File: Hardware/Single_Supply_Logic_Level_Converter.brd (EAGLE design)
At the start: 27.9 x 29.2 mm, 81 parts, among them U1 TXB0104, U2 TPS61200, U3 ADJ

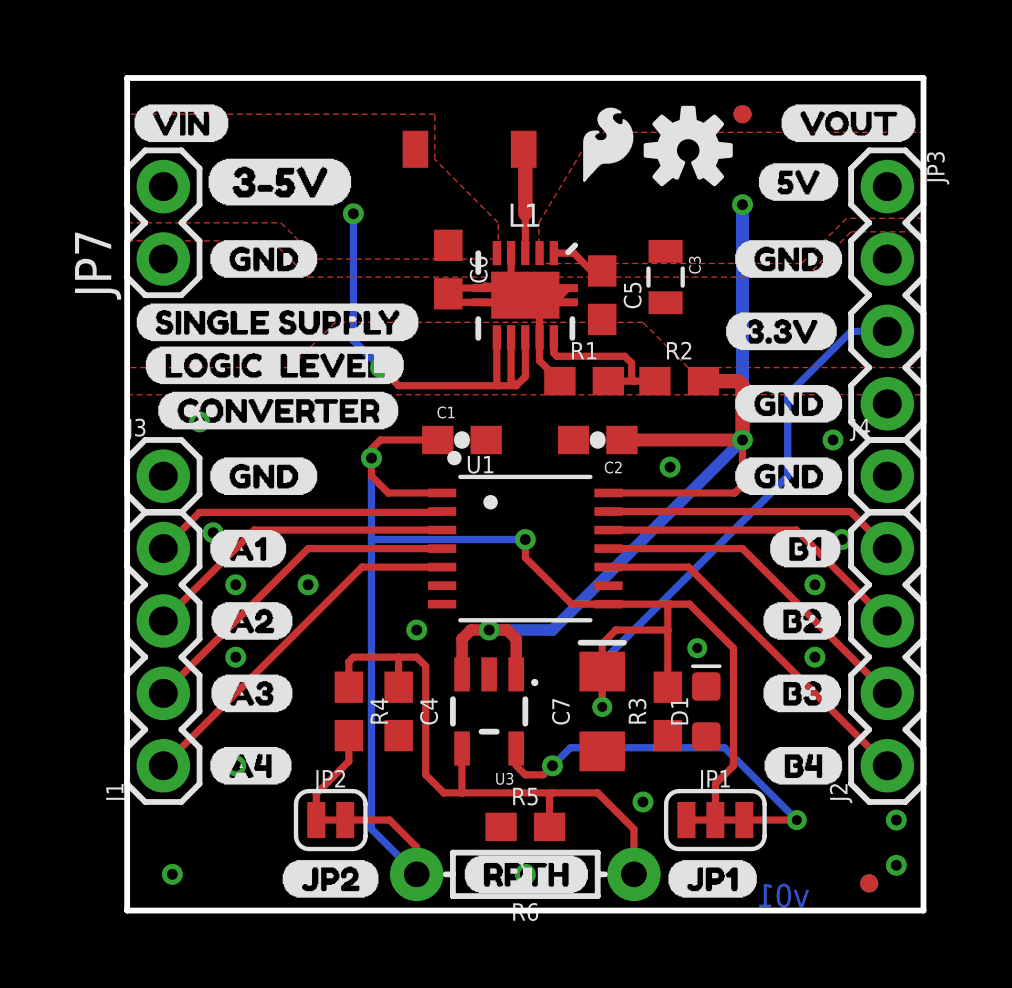
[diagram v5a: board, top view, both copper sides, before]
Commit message: Added text for warnings and jumper settings
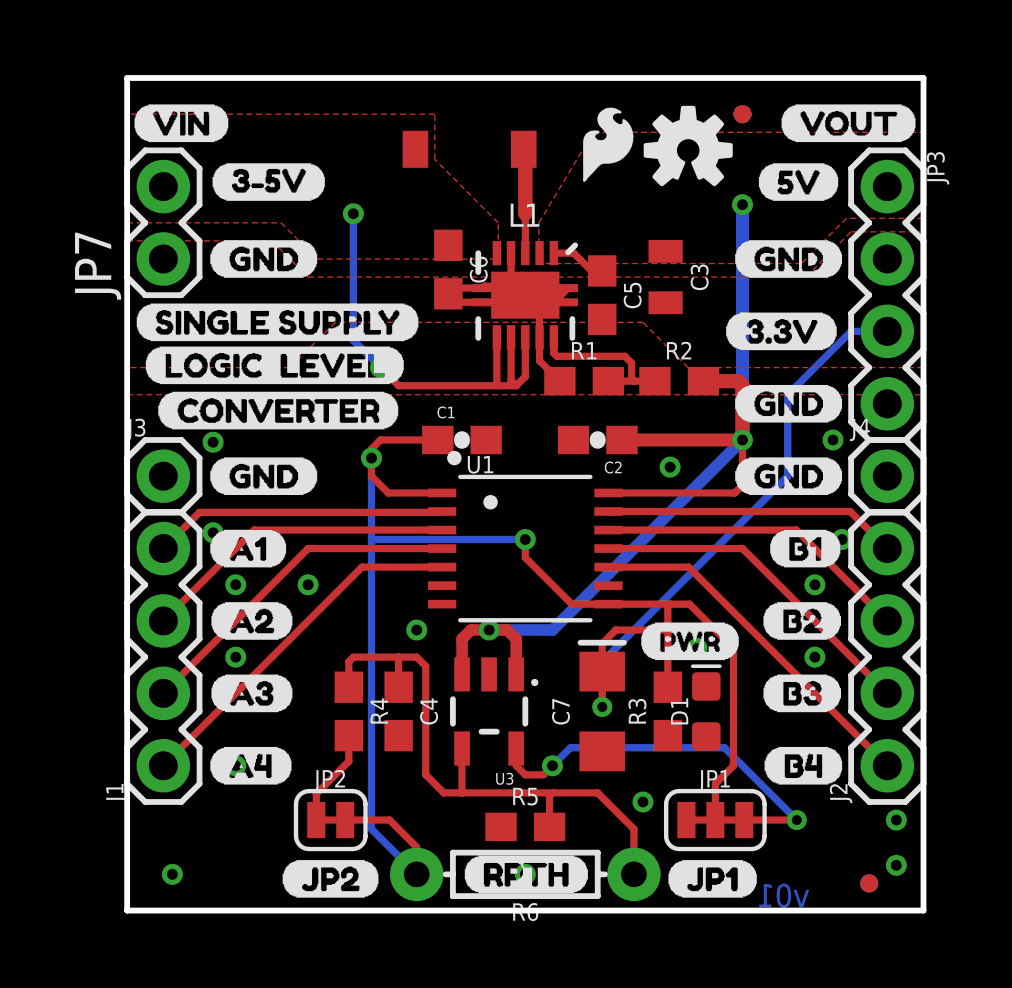
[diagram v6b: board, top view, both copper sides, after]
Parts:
- C3: device CH_passive:0805 -> SparkFun-Capacitors:0805
- U$25: device voltageIn:3#5V0 -> buzzard_labels (22):3#5V1
- U$29: device voltageIn:3#5V0 -> buzzard_labels (24):PWR0
- moved U$29 19.0 mm to (17.9, 9.45), flipped to the top
- moved U$25 0.16 mm to (2.94, 25.6)
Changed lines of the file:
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@@
 </autorouter>
 <elements>
-<element name="U1" library="SparkFun-IC-Comms" library_urn="urn:adsk.eagle:library:521" package="TSSOP14" package3d_urn="urn:adsk.eagle:package:38732/1" value="TXB0104" x="13.97" y="12.7" rot="R270">
-<attribute name="PROD_ID" value="NA-XXXXX" x="1.27" y="-5.08" size="1.778" layer="27" rot="R270" display="off"/>
+<element name="U1" library="SparkFun-IC-Comms" package="TSSOP14" value="TXB0104" x="13.97" y="12.7" rot="R270">
+<attribute name="PROD_ID" value="IC-13929" x="1.27" y="-5.08" size="1.778" layer="27" rot="R270" display="off"/>
 <attribute name="VALUE" value="TXB0104" x="13.97" y="12.7" size="1.778" layer="27" rot="R270" display="off"/>
 </element>
@@
 <attribute name="PROD_ID" value="CAP-00810" x="-2.54" y="40.64" size="1.778" layer="27" rot="R180" display="off"/>
 </element>
-<element name="C3" library="CH_passive" package="0805" value="22uF" x="18.89125" y="22.225" rot="R270"/>
+<element name="C3" library="SparkFun-Capacitors" package="0805" value="22uF" x="18.89125" y="22.225" rot="R270">
+<attribute name="PROD_ID" value="CAP-08402" x="18.89125" y="22.225" size="1.778" layer="27" rot="R270" display="off"/>
+<attribute name="VALUE" value="22uF" x="18.89125" y="22.225" size="1.778" layer="27" rot="R270" display="off"/>
+</element>
 <element name="U2" library="SparkFun-IC-Power" package="QFN-10_PAD" value="TPS61200" x="13.97" y="21.59" rot="R180">
 <attribute name="PROD_ID" value="IC-10035" x="13.97" y="21.59" size="1.778" layer="27" rot="R180" display="off"/>
 </element>
 <element name="C5" library="SparkFun-Capacitors" package="0603" value="0.1uF" x="16.66875" y="21.59" rot="R270">
-<attribute name="PROD_ID" value="CAP-08604" x="16.66875" y="21.59" size="1.778" layer="27" rot="R270" display="off"/>
+<attribute name="PROD_ID" value="CAP-00810" x="16.66875" y="21.59" size="1.778" layer="27" rot="R270" display="off"/>
 <attribute name="VALUE" value="0.1uF" x="16.66875" y="21.59" size="1.778" layer="27" rot="R270" display="off"/>
 </element>
@@
 </element>
 <element name="R4" library="SparkFun-Resistors" package="0603" value="13k" x="7.77875" y="6.985" rot="R270">
-<attribute name="PROD_ID" value="RES-09571" x="7.77875" y="6.985" size="1.778" layer="27" rot="R270" display="off"/>
+<attribute name="PROD_ID" value="RES-14017" x="7.77875" y="6.985" size="1.778" layer="27" rot="R270" display="off"/>
 </element>
 <element name="R5" library="SparkFun-Resistors" package="0603" value="22k" x="13.97" y="2.936875">
@@
 <element name="U$52" library="Single_Supply_Logic_Level_Converter_Lables" package="VOUT2" value="" x="27.78125" y="27.6225" rot="MR0"/>
 <element name="U$53" library="Single_Supply_Logic_Level_Converter_Lables" package="SINGLE_SUPPLY17" value="" x="18.335625" y="18.0975" rot="MR0"/>
-<element name="U$25" library="voltageIn" package="3#5V0" value="" x="2.778125" y="25.55875"/>
-<element name="U$29" library="voltageIn" package="3#5V0" value="" x="7.9375" y="25.55875" rot="MR0"/>
+<element name="U$25" library="buzzard_labels (22)" package="3#5V1" value="" x="2.936875" y="25.55875"/>
+<element name="U$29" library="buzzard_labels (24)" package="PWR0" value="" x="17.93875" y="9.445625"/>
 </elements>
 <signals>
@@
 <wire x1="15.47" y1="21.34" x2="14.5375" y2="21.34" width="0.254" layer="1"/>
 <wire x1="14.5375" y1="21.34" x2="14.2875" y2="21.59" width="0.254" layer="1"/>
-<via x="2.54" y="17.145" extent="1-16" drill="0.381"/>
+<via x="3.01625" y="16.430625" extent="1-16" drill="0.381"/>
 <via x="19.05" y="15.5575" extent="1-16" drill="0.381"/>
 <via x="24.765" y="16.51" extent="1-16" drill="0.381"/>

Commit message: adding buzzard labels
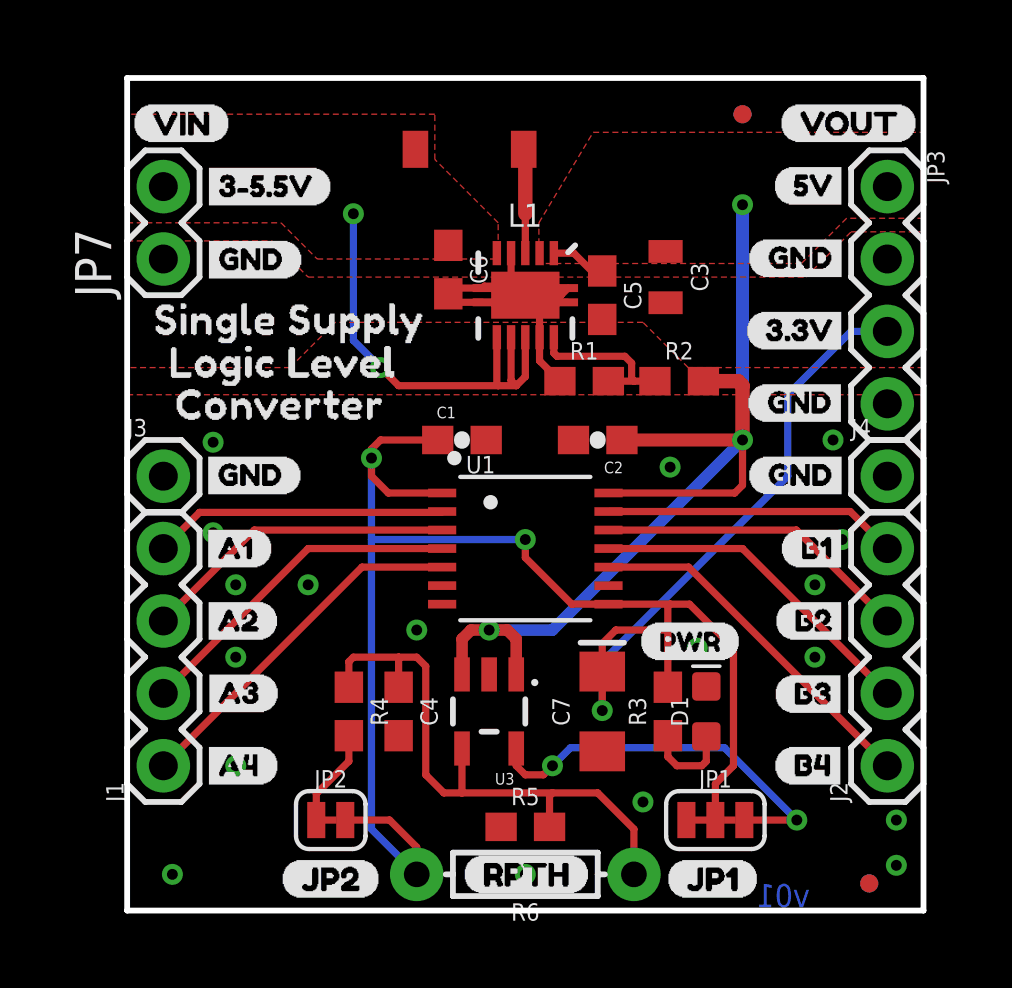
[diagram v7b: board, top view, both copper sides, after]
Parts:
- removed LOGO3: SFE_LOGO_FLAME.1_INCH, SparkFun-Aesthetics:SFE_LOGO_FLAME_.1
- removed LOGO4: OSHW-LOGOS, SparkFun-Aesthetics:OSHW-LOGO-S
- removed U$47, U$48, U$50: (no value), Single_Supply_Logic_Level_Converter_Lables:GND0
- removed U$49: (no value), Single_Supply_Logic_Level_Converter_Lables:3#3V20
- removed U$51: (no value), Single_Supply_Logic_Level_Converter_Lables:5V3
- removed U$53: (no value), Single_Supply_Logic_Level_Converter_Lables:SINGLE_SUPPLY17
- added U$34: (no value), buzzard_labels (49):A10
- added U$54: (no value), buzzard_labels (38):B19
- added U$55: (no value), buzzard_labels (38):B210
- added U$56: (no value), buzzard_labels (38):B311
- added U$57: (no value), buzzard_labels (38):B412
- added U$59: (no value), buzzard_labels (43):B13
- added U$61: (no value), buzzard_labels (43):B34
- U$10: device Single_Supply_Logic_Level_Converter_Lables:A16 -> buzzard_labels (42):CONVERTER0
- U$11: device Single_Supply_Logic_Level_Converter_Lables:A27 -> buzzard_labels (42):LOGIC_LEVEL2
- U$12: device Single_Supply_Logic_Level_Converter_Lables:A38 -> buzzard_labels (42):SINGLE_SUPPLY1
- U$13: device Single_Supply_Logic_Level_Converter_Lables:A49 -> buzzard_labels (38):GND3
- U$14: device Single_Supply_Logic_Level_Converter_Lables:B110 -> buzzard_labels (38):GND0
- U$15: device Single_Supply_Logic_Level_Converter_Lables:B211 -> buzzard_labels (38):GND3
- U$16: device Single_Supply_Logic_Level_Converter_Lables:B312 -> buzzard_labels (43):3#3V2
- U$17: device Single_Supply_Logic_Level_Converter_Lables:B413 -> buzzard_labels (43):3#5#5V6
- U$18: device Single_Supply_Logic_Level_Converter_Lables:CONVERTER19 -> buzzard_labels (38):3#3V4
- U$19: device Single_Supply_Logic_Level_Converter_Lables:GND0 -> buzzard_labels (38):5V2
- U$22: device Single_Supply_Logic_Level_Converter_Lables:LOGIC__LEVEL18 -> buzzard_labels (38):GND0
- U$24: device Single_Supply_Logic_Level_Converter_Lables:SINGLE_SUPPLY17 -> buzzard_labels (38):GND3
- U$25: device buzzard_labels (22):3#5V1 -> buzzard_labels (38):GND3
- U$26: device Single_Supply_Logic_Level_Converter_Lables:GND0 -> buzzard_labels (38):A15
- U$30: device Single_Supply_Logic_Level_Converter_Lables:GND0 -> buzzard_labels (38):A26
- U$31: device Single_Supply_Logic_Level_Converter_Lables:GND0 -> buzzard_labels (38):A37
- U$32: device Single_Supply_Logic_Level_Converter_Lables:GND0 -> buzzard_labels (38):A48
- U$33: device Single_Supply_Logic_Level_Converter_Lables:GND0 -> buzzard_labels (43):5V10
- U$35: device Single_Supply_Logic_Level_Converter_Lables:LOGIC__LEVEL18 -> buzzard_labels (49):A21
- U$36: device Single_Supply_Logic_Level_Converter_Lables:CONVERTER19 -> buzzard_labels (46):B43
- U$37: device Single_Supply_Logic_Level_Converter_Lables:GND0 -> buzzard_labels (46):B21
- U$38: device Single_Supply_Logic_Level_Converter_Lables:A16 -> buzzard_labels (38):GND3
- U$39: device Single_Supply_Logic_Level_Converter_Lables:A27 -> buzzard_labels (38):GND0
- U$40: device Single_Supply_Logic_Level_Converter_Lables:A38 -> buzzard_labels (38):GND0
- U$41: device Single_Supply_Logic_Level_Converter_Lables:A49 -> buzzard_labels (49):A32
- U$42: device Single_Supply_Logic_Level_Converter_Lables:B413 -> buzzard_labels (49):A43
- U$43: device Single_Supply_Logic_Level_Converter_Lables:B312 -> buzzard_labels (42):CONVERTER0
- U$45: device Single_Supply_Logic_Level_Converter_Lables:B211 -> buzzard_labels (42):LOGIC_LEVEL2
- U$46: device Single_Supply_Logic_Level_Converter_Lables:B110 -> buzzard_labels (42):SINGLE_SUPPLY1
- U$7: device Single_Supply_Logic_Level_Converter_Lables:3#3V20 -> buzzard_labels (38):3#5#5V1
- U$9: device Single_Supply_Logic_Level_Converter_Lables:5V3 -> buzzard_labels (38):GND0
- moved U$13 26.0 mm to (21.8, 22.9)
- moved U$17 25.5 mm to (6.86, 25.4), flipped to the bottom
- moved U$32 22.7 mm to (2.49, 5.08)
- moved U$24 22.2 mm to (21.8, 15.3)
- moved U$40 22.0 mm to (25.4, 17.8)
- moved U$18 20.8 mm to (21.7, 20.3)
- moved U$15 20.7 mm to (5.84, 22.9), flipped to the bottom
- moved U$25 20.3 mm to (21.7, 17.8)
- moved U$31 20.3 mm to (2.46, 7.62)
- moved U$39 20.2 mm to (25.4, 15.2)
- moved U$42 20.2 mm to (5.00, 5.08)
- moved U$19 19.9 mm to (22.6, 25.4)
- moved U$9 19.8 mm to (2.49, 22.8)
- moved U$37 19.3 mm to (25.4, 10.2)
- moved U$7 19.2 mm to (2.49, 25.4)
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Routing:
- net N$3: track 0.00 -> 3.15 mm

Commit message: changing voltage output programming
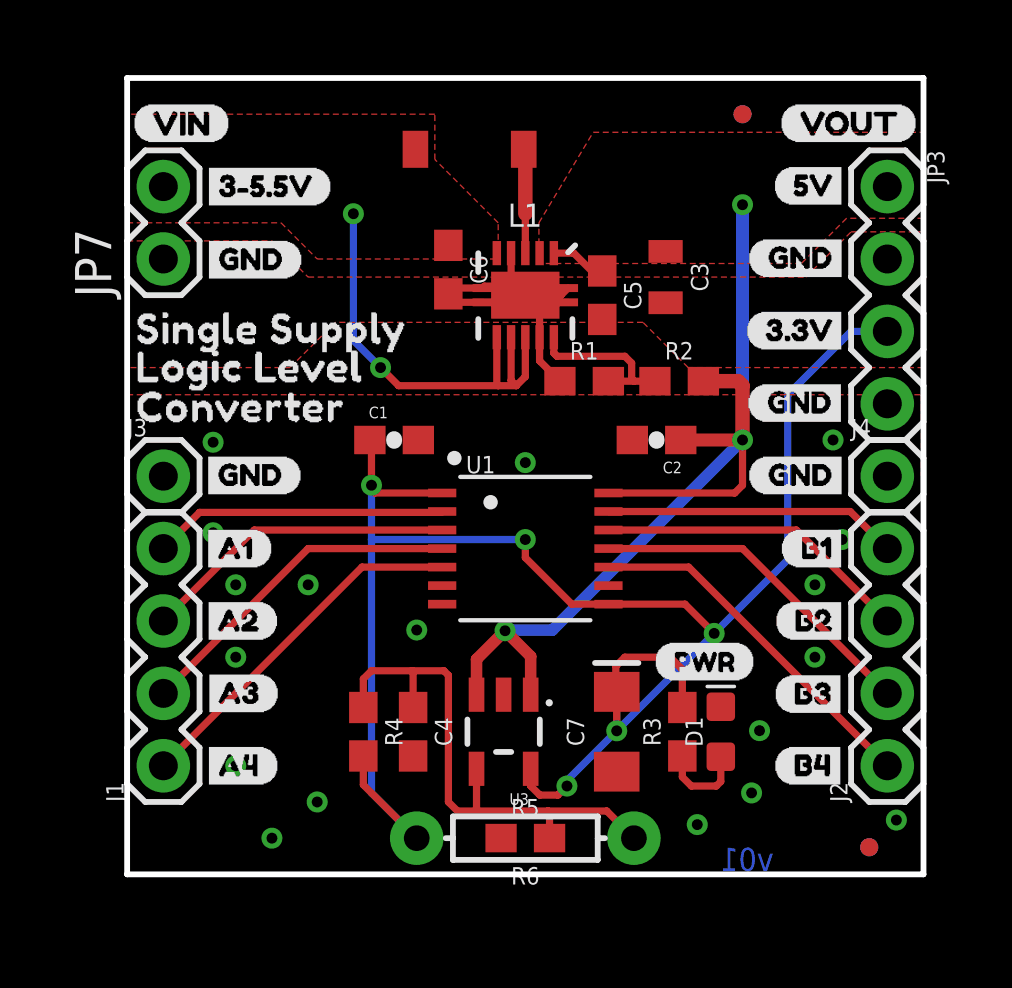
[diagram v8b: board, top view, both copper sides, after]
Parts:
- removed JP1: JUMPER-SMT_3_1-NC_TRACE_SILK, SparkFun-Jumpers:SMT-JUMPER_3_1-NC_TRACE_SILK
- removed JP2: JUMPER-SMT_2_NC_TRACE_SILK, SparkFun-Jumpers:SMT-JUMPER_2_NC_TRACE_SILK
- removed U$20: (no value), Single_Supply_Logic_Level_Converter_Lables:JP114
- removed U$21: (no value), Single_Supply_Logic_Level_Converter_Lables:JP215
- removed U$23, U$44: (no value), Single_Supply_Logic_Level_Converter_Lables:RPTH16
- moved C1 2.38 mm to (9.37, 16.5)
- moved C2 2.06 mm to (18.6, 16.5)
- moved U$10 1.37 mm to (-0.64, 17.7)
- moved FD3 1.27 mm to (26.0, 2.22)
- moved FD4 1.27 mm to (26.0, 2.22)
- moved R6 1.27 mm to (14.0, 2.54)
- moved U$11 1.17 mm to (-0.63, 19.1)
- moved R3 0.87 mm to (19.5, 6.27)
- moved U$29 0.87 mm to (18.4, 8.73)
- moved U3 0.87 mm to (13.2, 6.27)
- moved R4 0.87 mm to (8.29, 6.27)
- moved C4 0.87 mm to (10.0, 6.27)
- moved C7 0.87 mm to (17.2, 6.27)
- moved D1 0.87 mm to (20.8, 6.27)
- moved LOGO2 0.87 mm to (14.5, 8.24)
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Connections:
- removed net N$1: JP1.3, U3.5
- removed net N$12: JP2.1, R4.2
- net VCCA: now also R4.2, U3.5; no longer JP1.1, JP1.2, JP2.2
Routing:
- net N$1: track 13.9 -> 0.00 mm, vias 2 -> 0
- net VCCA: track 73.2 -> 66.8 mm, vias 3 -> 5
- net N$12: track 3.48 -> 0.00 mm
- net 5V: track 38.6 -> 36.7 mm
- net N$11: track 21.1 -> 19.4 mm
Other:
- board size 27.9 x 29.2 mm -> 27.9 x 27.9 mm
